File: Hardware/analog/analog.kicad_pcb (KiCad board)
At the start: 4 copper layers, 128 x 182 mm, 129 parts, among them J201 Würth 74651194R, J202 Würth 74651194R, J301 Conn_02x10_Odd_Even, J501 Conn_01x01, J502 Conn_01x01, M501 Fan_4pin, Q201 IXTH80N075L2, Q202 IXTH80N075L2, Q501 MMBT3904, U201 ADA4522-2, U202 LM431SC, U203 LMT86LMT, U204 ADA4522-2, U205 LM431SC, U301 ADUM131D, U302 ADUM131D, U303 ADUM1250, U304 74LVC1G19, U305 AT24CS32-SSHM, U401 ICL7660, U402 MCP1804x-C002xMB, U403 MCP1703AT-5002E/DB, U404 XC6203E33, U405 LP5907MFX-3.3, U501 EMC2101-R, U601 MCP3562, U602 MAX6166, U603 DAC8562, U701 Si5351A-B-GT, Y701 25MHz

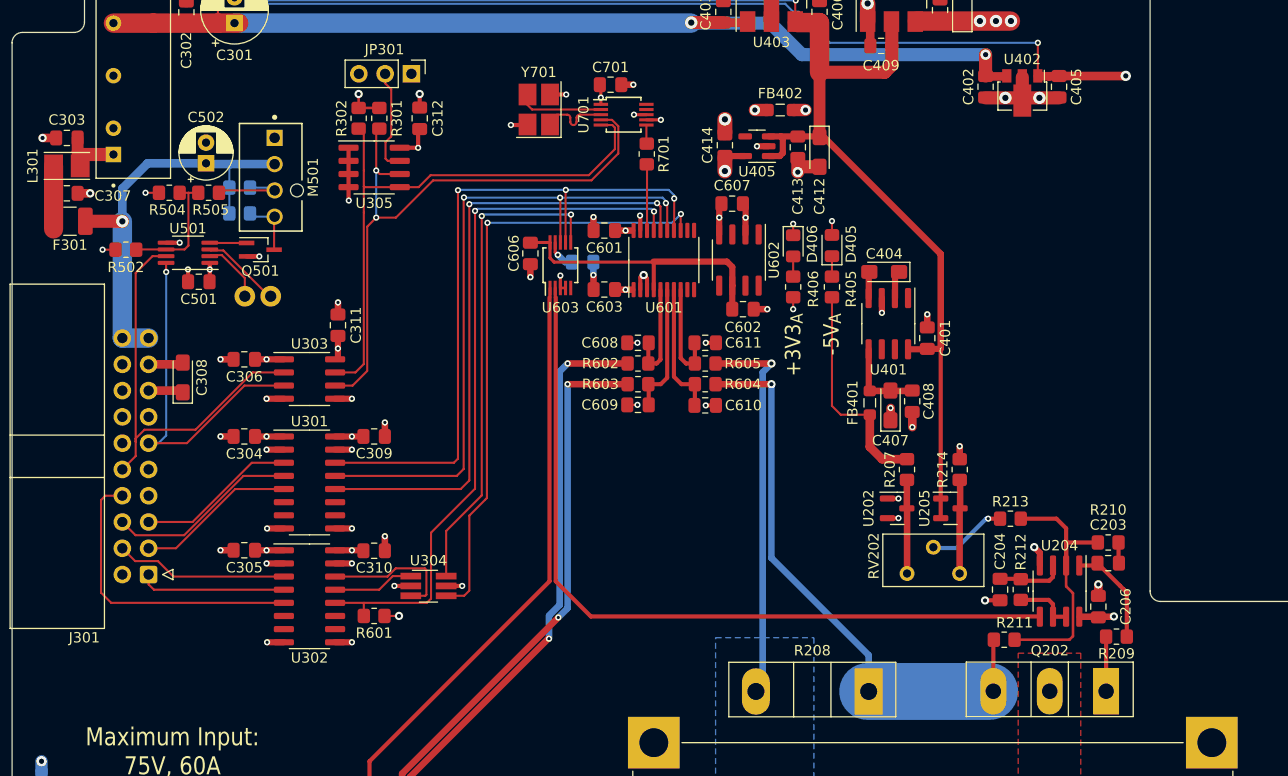
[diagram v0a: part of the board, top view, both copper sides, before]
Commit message: Added more decoupling for reference
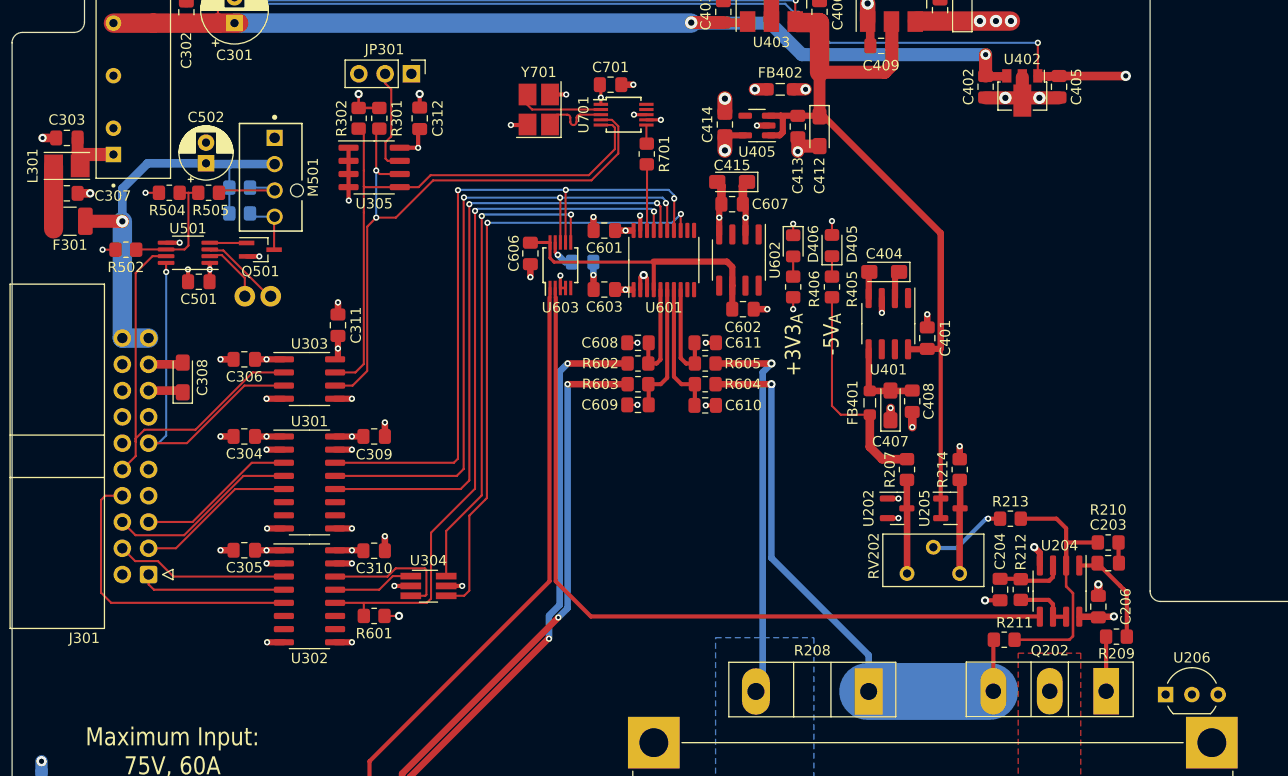
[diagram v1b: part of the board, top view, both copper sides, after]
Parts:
- added C415: 10µF, Capacitor_Tantalum_SMD:CP_EIA-3216-18_Kemet-A_Pad1.58x1.35mm_HandSolder, F.Cu at (89.6, 89.5)
- added U206: LMT86LMT, Package_TO_SOT_THT:TO-92_Inline_Wide, F.Cu at (131.5, 139.0)
- moved C412 2.00 mm to (98.0, 84.5)
- moved C413 2.00 mm to (96.0, 84.1)
- moved C414 2.00 mm to (88.9, 83.9)
- moved FB402 2.00 mm to (94.2, 80.5)
- moved U405 2.00 mm to (92.0, 84.0)
- moved C607 0.05 mm to (89.6, 91.6)
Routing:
- net GNDA: track 17.4 -> 19.7 mm
- net +3V3A: track 11.9 -> 14.1 mm

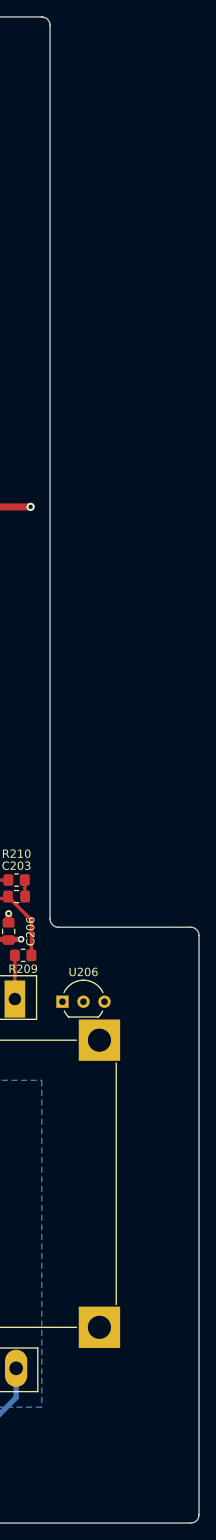
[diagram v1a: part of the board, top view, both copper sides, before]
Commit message: Cleaning up controller schematic/board
- This moves a few things around but doesn't functionally change
  anything; mostly this is moving the files to the KiCad nightly format
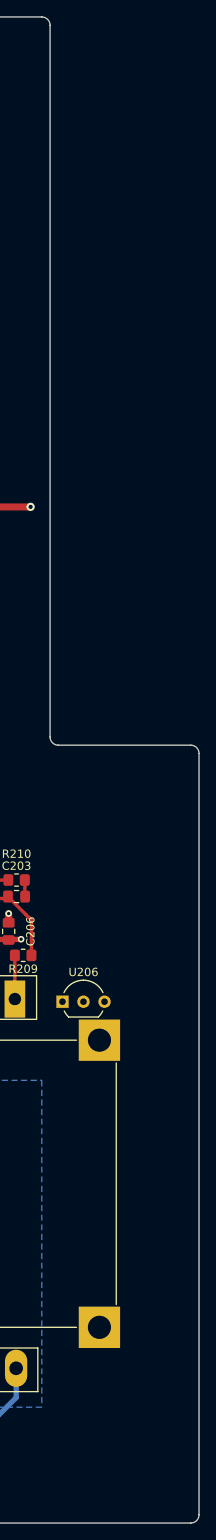
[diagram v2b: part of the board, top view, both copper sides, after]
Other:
- outline, holes or cut-outs redrawn
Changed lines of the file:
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@@
   (gr_line (start 21 20) (end 129 20)
     (stroke (width 0.1) (type solid)) (layer "Edge.Cuts"))
-  (gr_line (start 148 131) (end 148 201)
+  (gr_line (start 148 109) (end 148 201)
     (stroke (width 0.1) (type solid)) (layer "Edge.Cuts"))
   (gr_arc (start 129 20) (mid 129.707107 20.292893) (end 130 21)
     (stroke (width 0.1) (type solid)) (layer "Edge.Cuts"))
-  (gr_arc (start 131 130) (mid 130.292893 129.707107) (end 130 129)
+  (gr_arc (start 131 108) (mid 130.292893 107.707107) (end 130 107)
     (stroke (width 0.1) (type solid)) (layer "Edge.Cuts"))
   (gr_arc (start 20 76) (mid 20.292893 75.292893) (end 21 75)
     (stroke (width 0.1) (type solid)) (layer "Edge.Cuts"))
-  (gr_line (start 131 130) (end 147 130)
+  (gr_line (start 131 108) (end 147 108)
     (stroke (width 0.1) (type solid)) (layer "Edge.Cuts"))
   (gr_arc (start 27 74) (mid 26.707107 74.707107) (end 26 75)
@@
   (gr_line (start 20 201) (end 20 76)
     (stroke (width 0.1) (type solid)) (layer "Edge.Cuts"))
-  (gr_arc (start 147 130) (mid 147.707107 130.292893) (end 148 131)
+  (gr_arc (start 147 108) (mid 147.707107 108.292893) (end 148 109)
     (stroke (width 0.1) (type solid)) (layer "Edge.Cuts"))
   (gr_arc (start 21 43) (mid 20.292893 42.707107) (end 20 42)
@@
   (gr_line (start 21 202) (end 147 202)
     (stroke (width 0.1) (type solid)) (layer "Edge.Cuts"))
-  (gr_line (start 130 21) (end 130 129)
+  (gr_line (start 130 21) (end 130 107)
     (stroke (width 0.1) (type solid)) (layer "Edge.Cuts"))
   (gr_arc (start 148 201) (mid 147.707107 201.707107) (end 147 202)
@@
     (polygon
       (pts
-        (xy 130 129)
-        (xy 131 130)
-        (xy 148 130)
+        (xy 130 107)
+        (xy 131 108)
+        (xy 148 108)
         (xy 148 202)
         (xy 20 202)
@@
     (polygon
       (pts
-        (xy 130 129)
-        (xy 131 130)
-        (xy 148 130)
+        (xy 130 107)
+        (xy 131 108)
+        (xy 148 108)
         (xy 148 202)
         (xy 20 202)

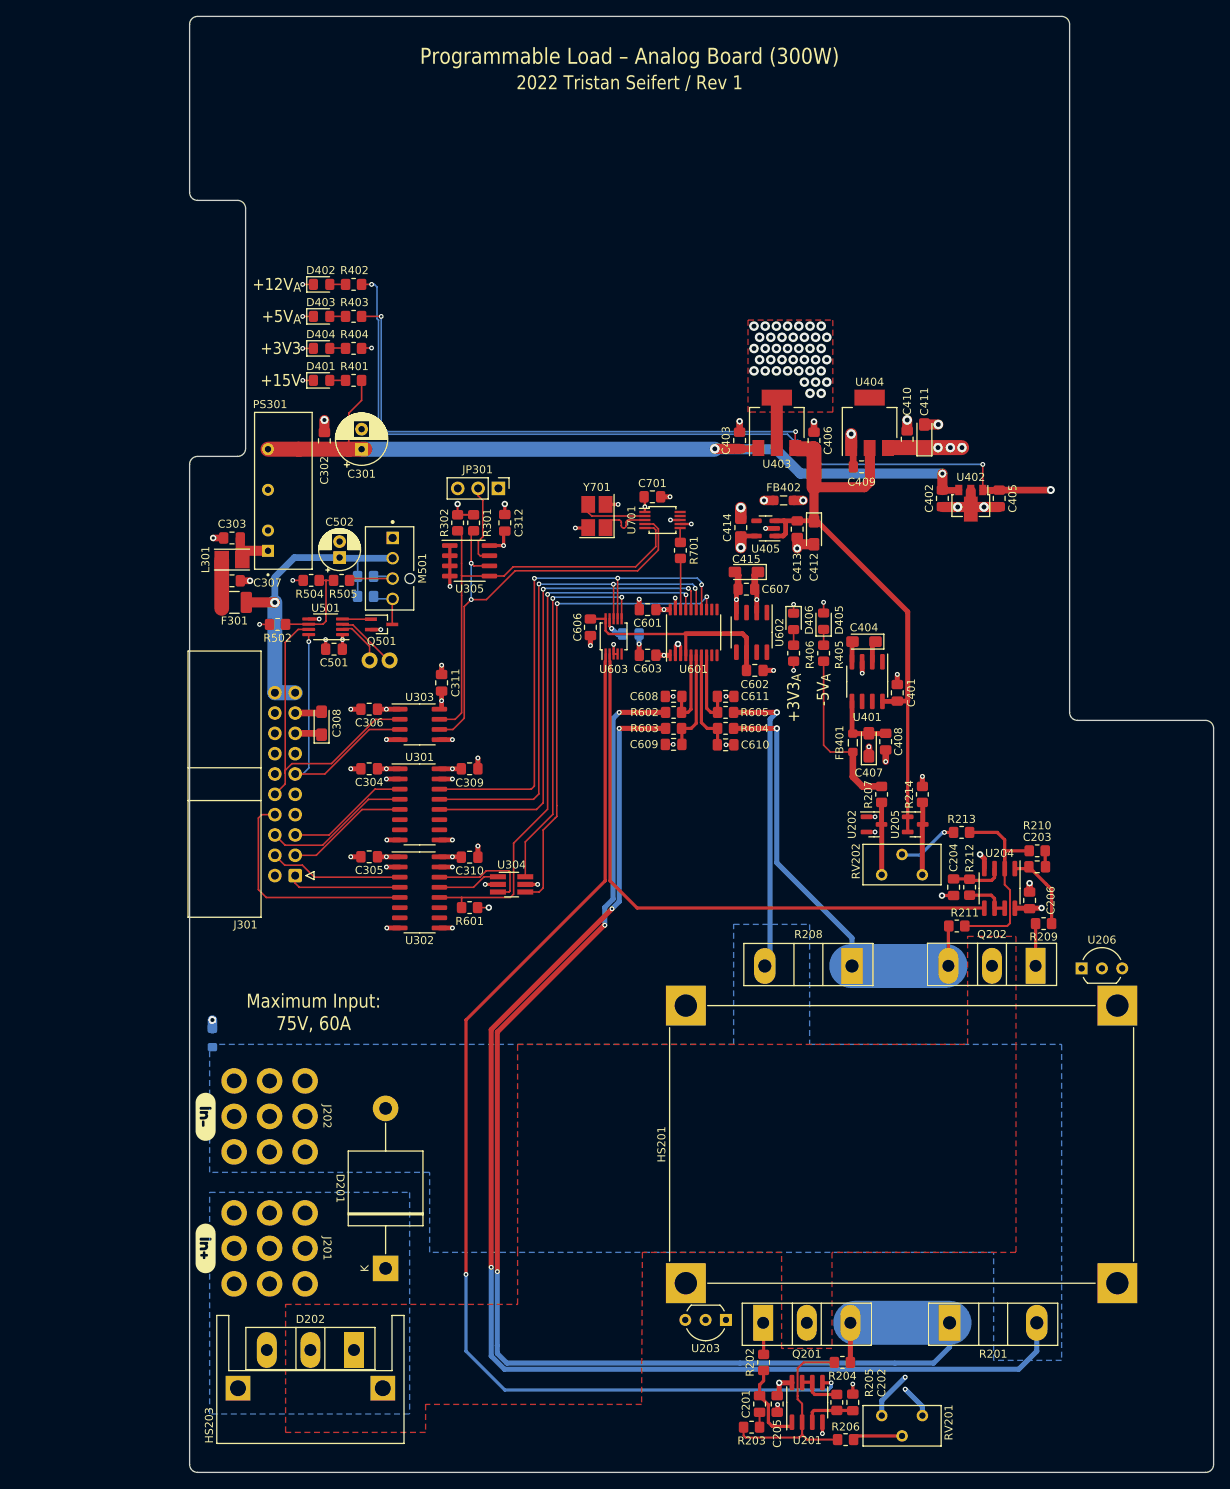
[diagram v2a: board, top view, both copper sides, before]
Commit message: More reworking of the controller and friends
- Add more rear IO to the controller, in this case finishing positioning
  of the Ethernet jack, and adding a suitable right angle USB B jack
  (USB C is preferrable but there's basically no jacks that are
  sufficiently long)

- Mostly finish power section on controller (save for the enable input
  for our +3V3 rail; it'll be slaved off the SoM +3V3 rail)

- Minor tweaks to pinout of FFC connector on front panel

- Update cutout shape of analog board

- Fixed a few footprints metadata

- Add footprints for further rear panel IO
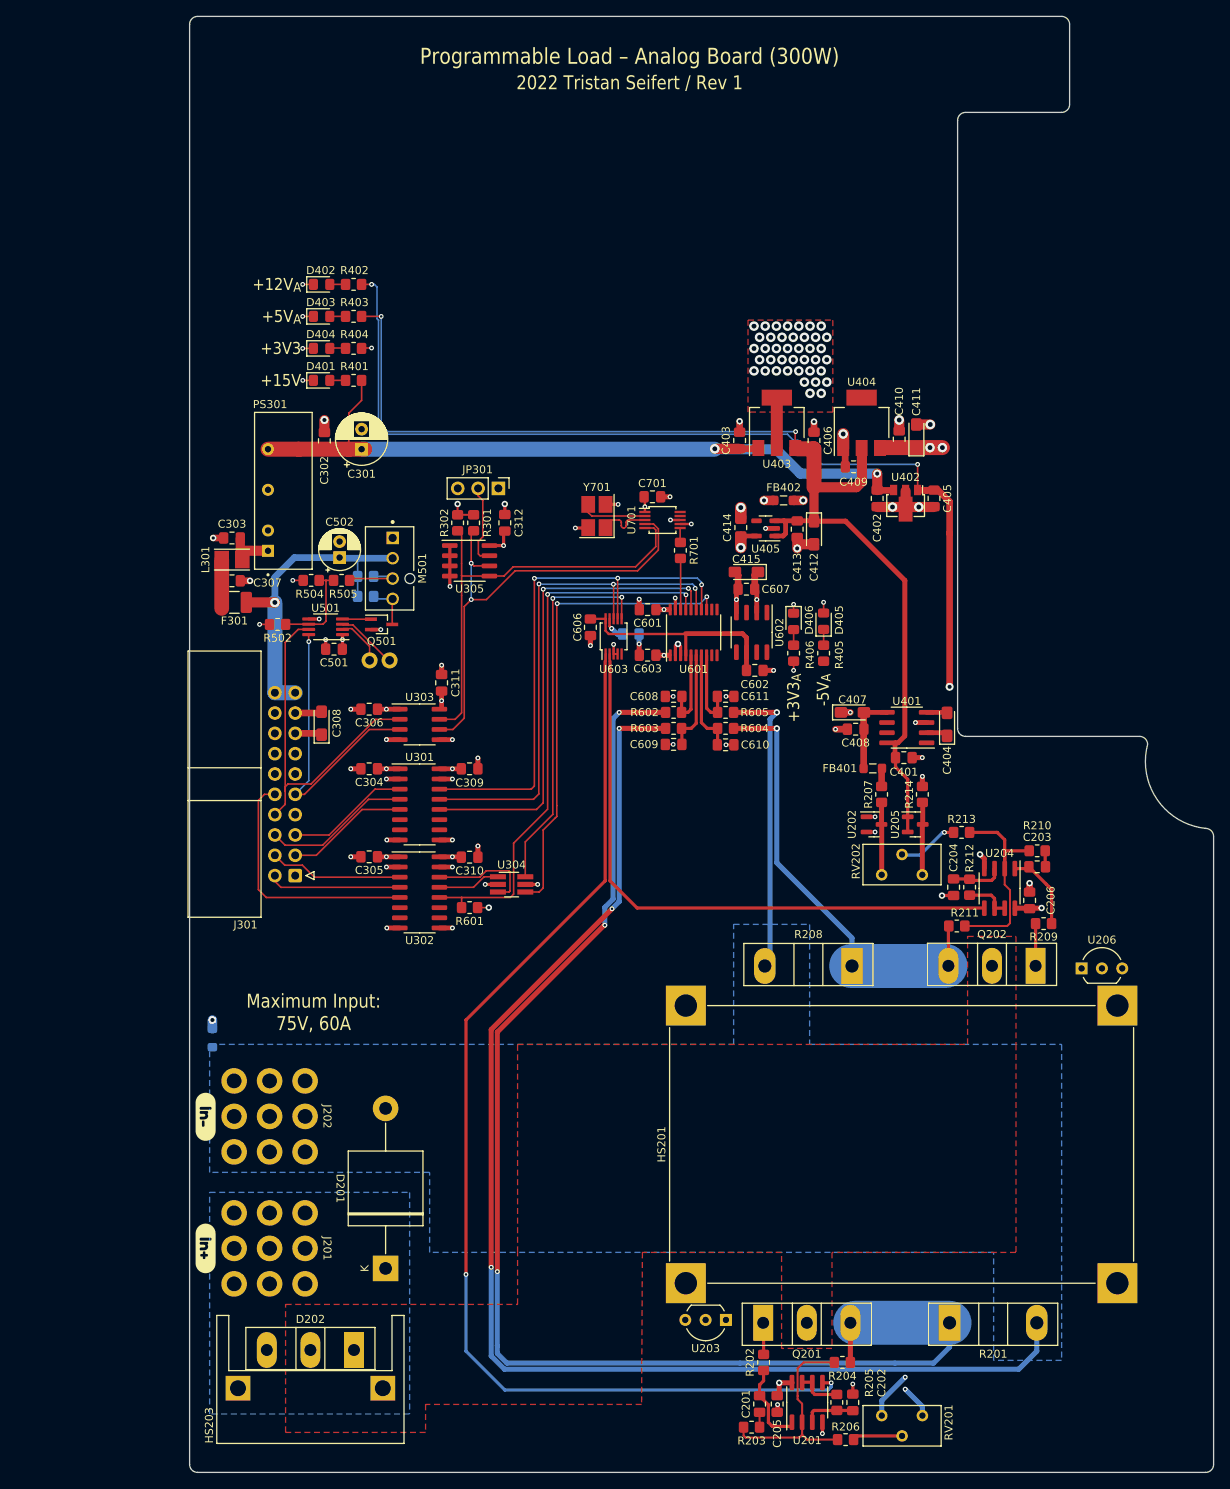
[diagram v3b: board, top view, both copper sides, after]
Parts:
- moved C404 14.7 mm to (114.7, 108.5), turned to 90 degrees
- moved C405 8.15 mm to (113.0, 80.2)
- moved U402 8.15 mm to (109.5, 80.8)
- moved C402 8.15 mm to (106.0, 80.2)
- moved C401 8.15 mm to (109.3, 112.7), turned to 0 degrees
- moved U401 7.59 mm to (109.7, 108.9), turned to 180 degrees
- moved C407 4.54 mm to (102.9, 107.0), turned to 0 degrees
- moved C408 4.06 mm to (103.3, 109.1), turned to 180 degrees
- moved FB401 4.06 mm to (105.4, 114.0), turned to 0 degrees
- moved C409 1.00 mm to (103.0, 76.3)
- moved C410 1.00 mm to (108.7, 72.8)
- moved C411 1.00 mm to (110.8, 72.5)
- moved U404 1.00 mm to (104.0, 70.8)
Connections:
- J301 pad 1: /External Interface/IN_SPI_SSEL0 -> /External Interface/IN_SPI_SSEL1
- J301 pad 10: IN_I2C_SDA -> /External Interface/~{OUT_IRQ}
- J301 pad 11: IN_I2C_SCL -> /External Interface/~{IN_RESET}
- J301 pad 2: /External Interface/IN_SPI_SSEL1 -> /External Interface/IN_SPI_SSEL0
- J301 pad 8: /External Interface/~{OUT_IRQ} -> IN_I2C_SDA
- J301 pad 9: /External Interface/~{IN_RESET} -> IN_I2C_SCL
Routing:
- net -5VA: track 21.2 -> 2.40 mm
- net +12VA: track 269.2 -> 260.0 mm
- net +15V: track 104.8 -> 96.6 mm
- net IN_I2C_SDA: track 40.4 -> 44.0 mm
- net IN_I2C_SCL: track 34.1 -> 37.1 mm
- net /External Interface/IN_SPI_SSEL0: track 14.2 -> 16.6 mm
- net /External Interface/~{OUT_IRQ}: track 29.3 -> 31.6 mm
- net Net-(U401-VOUT): track 8.05 -> 9.81 mm
- net +3V3: track 32.0 -> 30.6 mm, vias 14 -> 13
- net +5VA: track 148.1 -> 147.3 mm
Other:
- outline, holes or cut-outs redrawn
- board text added: "TODO: move connector"
- board text removed: "↑ Cutout for front panel jacks ↑"
